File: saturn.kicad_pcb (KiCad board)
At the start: 4 copper layers, 100 x 66 mm, 112 parts, among them J1 Conn_01x04_Pin, J10 Conn_01x04, J11 USB_B_Micro, J12 USB_C_Receptacle_USB2.0, J13 ZX-XH2.54-3PWT, J14 Conn_01x04_Pin, J2 PMOD3_FULL, J3 Conn_01x06, J4 Conn_01x06, J6 ZX-XH2.54-10PWT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

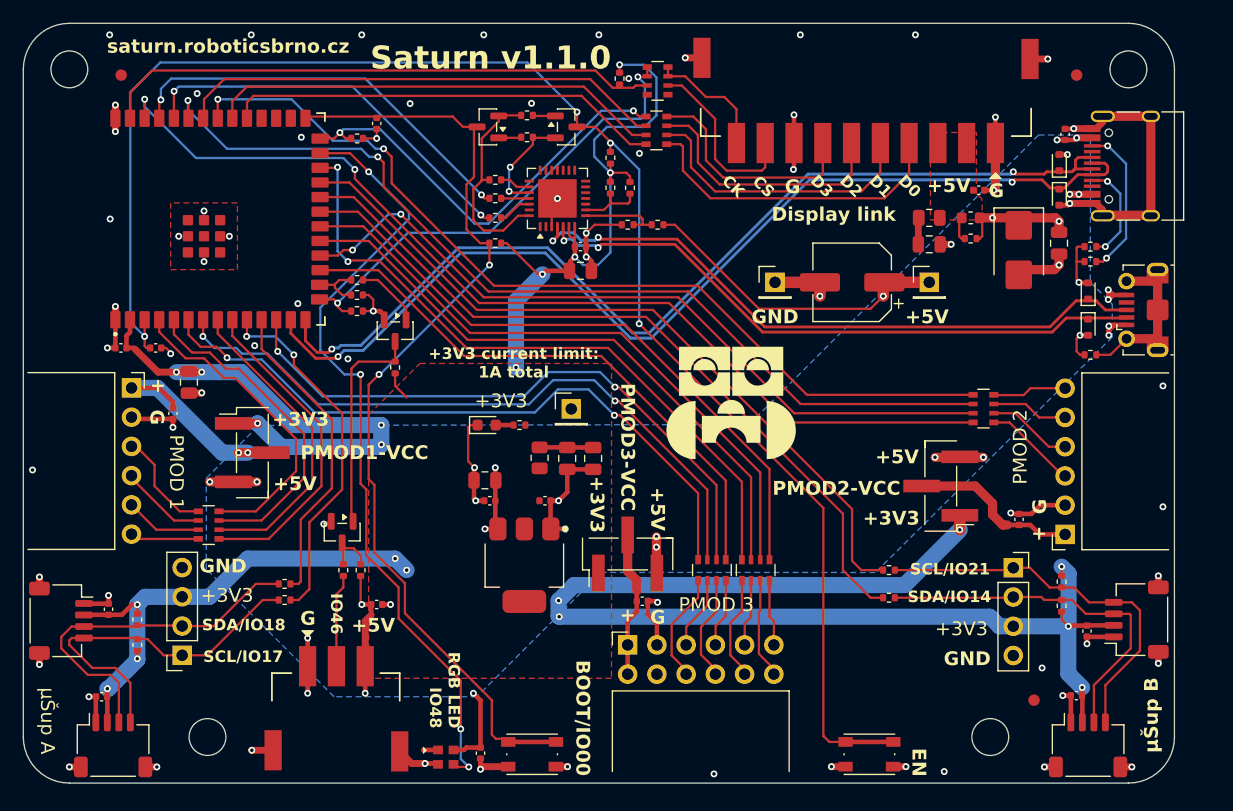
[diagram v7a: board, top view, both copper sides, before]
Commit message: Replace Micro-USB connector
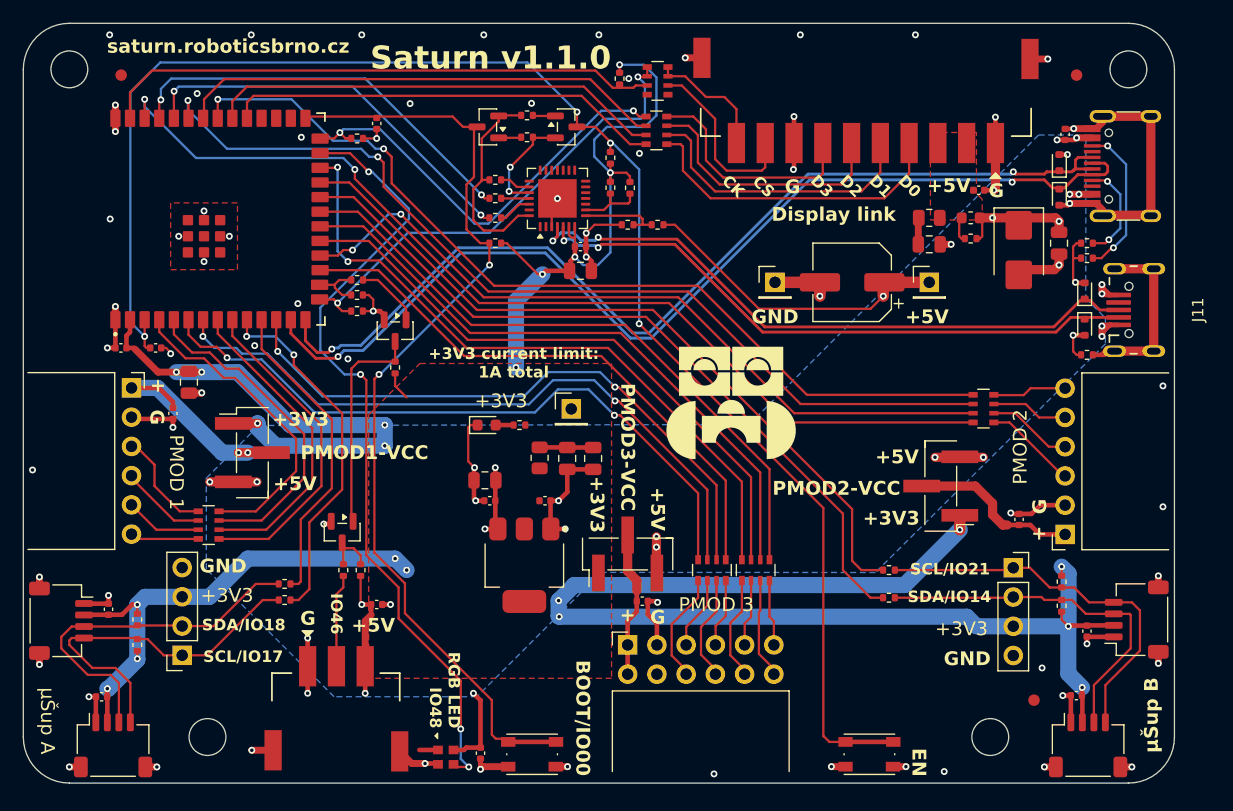
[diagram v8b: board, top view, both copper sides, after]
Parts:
- J11: value USB_B_Micro -> MICRO 4P DIP; footprint USB_Conn:USB_Micro-B_XNJ-073_With_THR_Paste -> USB_Conn:USB_MICRO 4P DIP
- J12: value USB_C_Receptacle_USB2.0 -> TYPE-C-31-M-12
- moved J11 0.80 mm to (141.5, 80.9)
- moved R70 0.42 mm to (137.4, 75.1)
- moved R69 0.42 mm to (137.4, 76.4)
- moved D8 0.30 mm to (137.2, 79.2)
- moved D9 0.30 mm to (137.2, 82.4)
- moved R71 0.30 mm to (137.4, 84.8)
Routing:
- net GND: track 160.8 -> 162.4 mm
- net +3V3: track 250.0 -> 250.8 mm
- net /USBAUX_D+: track 56.5 -> 55.8 mm
- net /USBAUX_D-: track 54.4 -> 53.7 mm
- net Net-(J11-Shield): track 15.4 -> 16.0 mm
